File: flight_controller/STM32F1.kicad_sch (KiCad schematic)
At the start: 26 parts, among them J2 HB-PH9-12727PB2GOB, SW2 6.0*6.0*6.0, U2 STM32F103C8T6, X3 X322524MLB4SI_C5210646

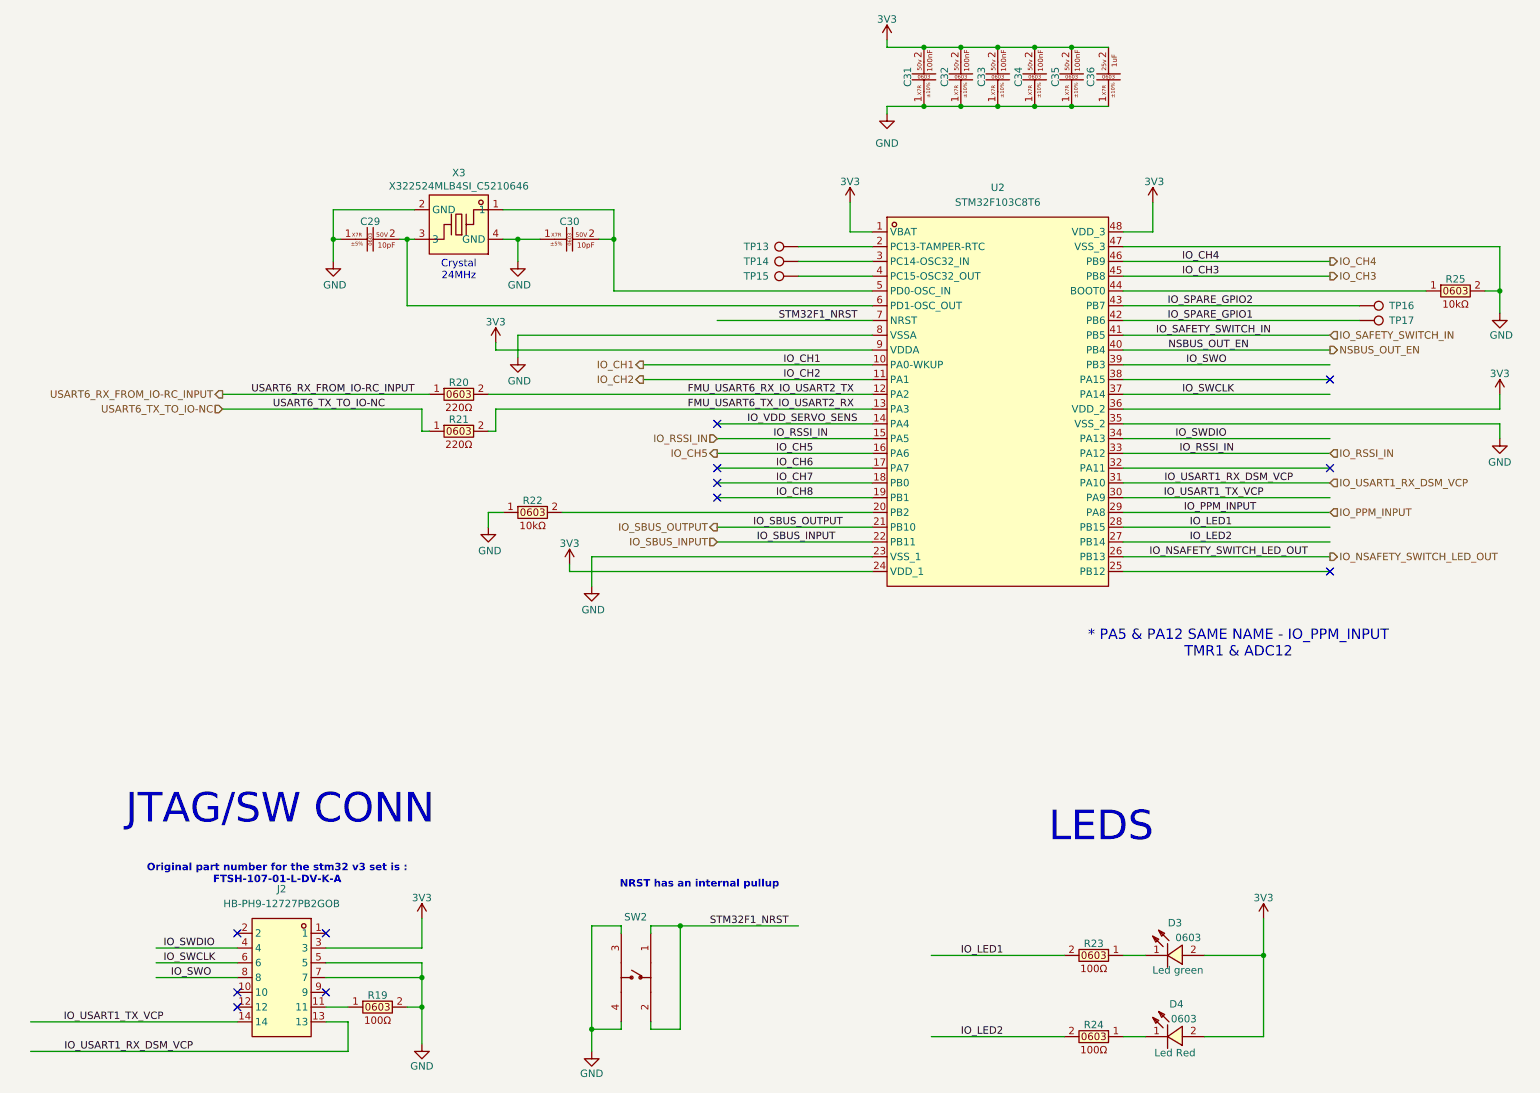
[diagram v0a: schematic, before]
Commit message: Revert to state of commit 2458262 moved all to components to top
Reverts commits: d012532, 3d9c600, 58bc0ac
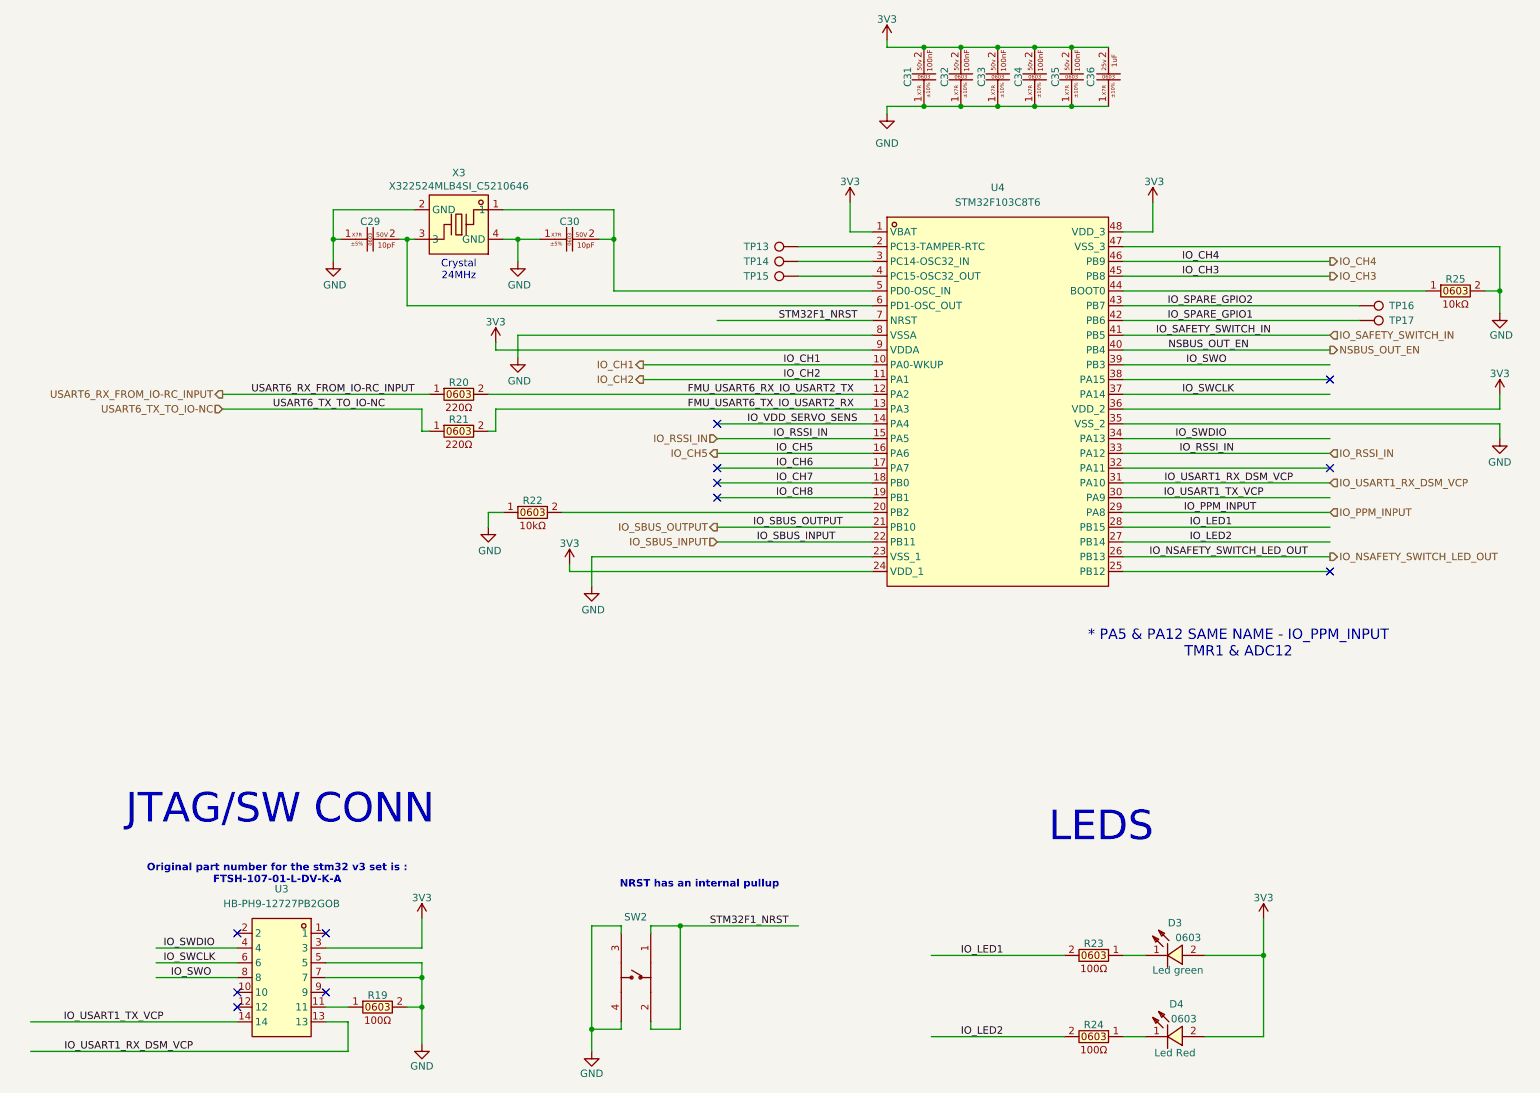
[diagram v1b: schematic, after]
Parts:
- renumbered J2 to U3, U2 to U4
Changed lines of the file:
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@@
 		(dnp no)
 		(fields_autoplaced yes)
-		(property "Reference" "U2"
+		(property "Reference" "U4"
 			(at 354.33 114.3 0)
 			(effects
@@
 			(project "FP_BOARD"
 				(path "/17737359-1a8e-4237-8899-d9604030bc1d/e4f0bf63-f781-4c4e-9f6b-c9f89551cbca"
-					(reference "U2")
+					(reference "U4")
 					(unit 1)
 				)
@@
 		(on_board yes)
 		(dnp no)
-		(property "Reference" "J2"
+		(property "Reference" "U3"
 			(at 231.14 234.95 0)
 			(effects
@@
 			(project "FP_BOARD"
 				(path "/17737359-1a8e-4237-8899-d9604030bc1d/e4f0bf63-f781-4c4e-9f6b-c9f89551cbca"
-					(reference "J2")
-					(unit 1)
-				)
+					(reference "U3")
+					(unit 1)
+				)

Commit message: Updated power and usb connectors, annotations and netlist check
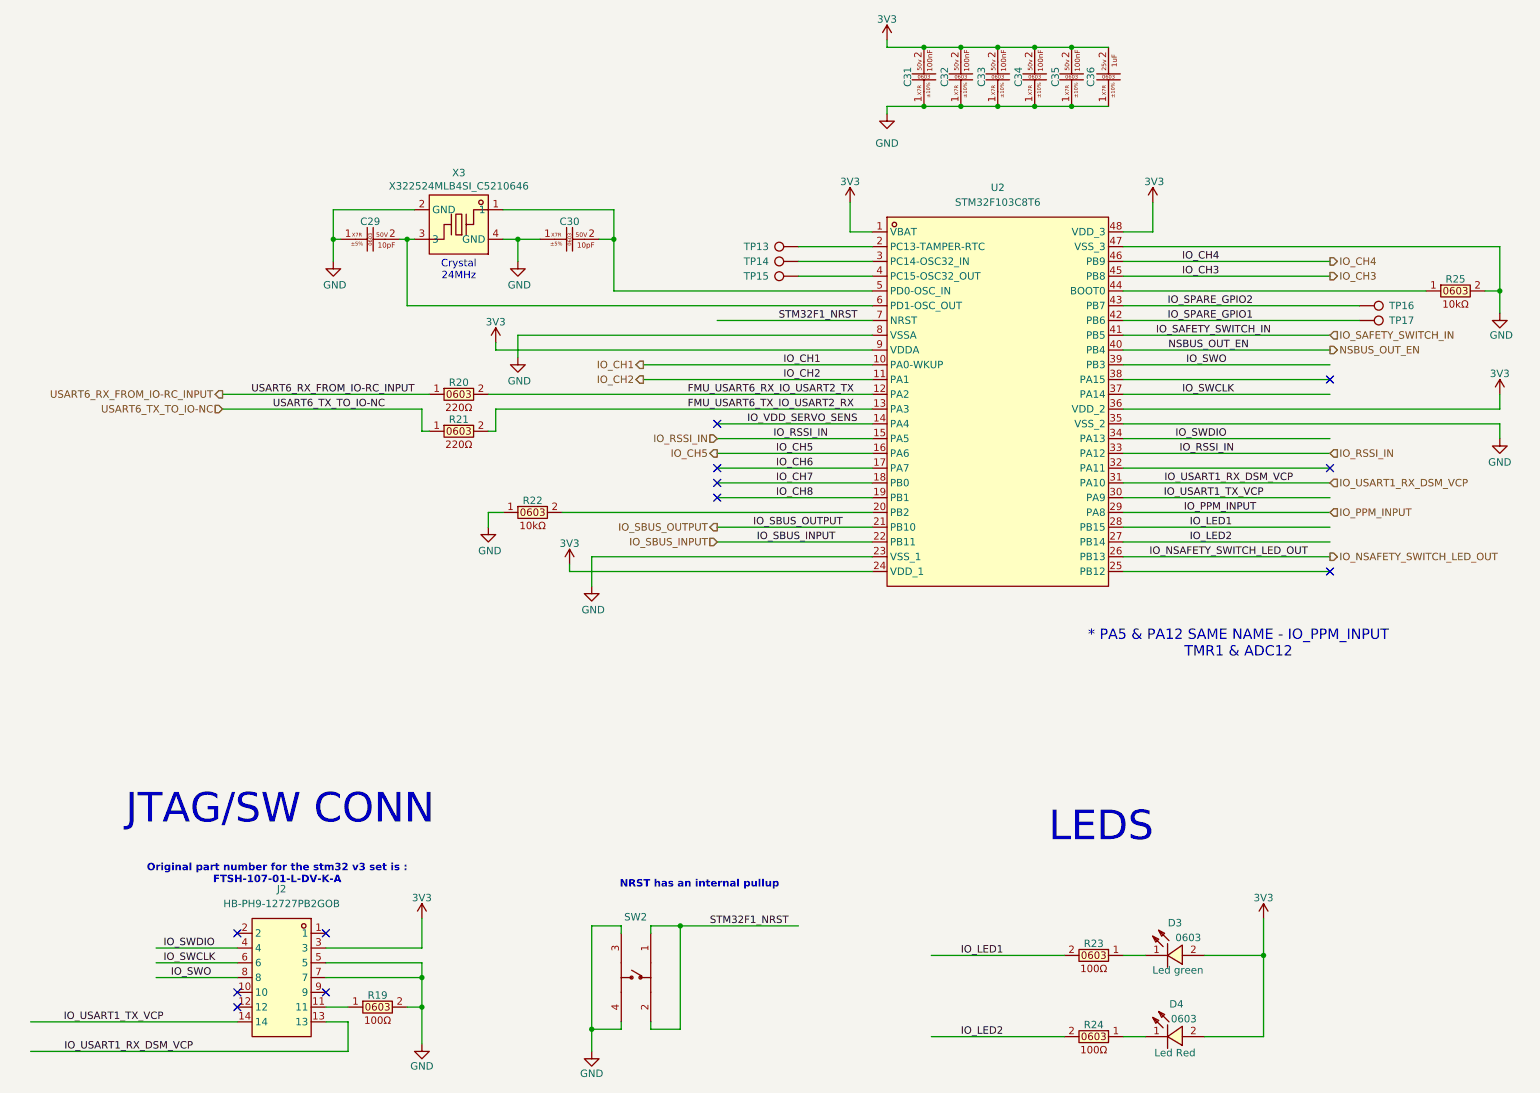
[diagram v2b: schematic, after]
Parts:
- renumbered U3 to J2, U4 to U2
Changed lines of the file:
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@@
 		(dnp no)
 		(fields_autoplaced yes)
-		(property "Reference" "U4"
+		(property "Reference" "U2"
 			(at 354.33 114.3 0)
 			(effects
@@
 			(project "FP_BOARD"
 				(path "/17737359-1a8e-4237-8899-d9604030bc1d/e4f0bf63-f781-4c4e-9f6b-c9f89551cbca"
-					(reference "U4")
+					(reference "U2")
 					(unit 1)
 				)
@@
 		(on_board yes)
 		(dnp no)
-		(property "Reference" "U3"
+		(property "Reference" "J2"
 			(at 231.14 234.95 0)
 			(effects
@@
 			(project "FP_BOARD"
 				(path "/17737359-1a8e-4237-8899-d9604030bc1d/e4f0bf63-f781-4c4e-9f6b-c9f89551cbca"
-					(reference "U3")
-					(unit 1)
-				)
+					(reference "J2")
+					(unit 1)
+				)
